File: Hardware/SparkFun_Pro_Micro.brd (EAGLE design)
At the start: 17.8 x 33 mm, 33 parts, among them U2 MIC5219, U3 ATMEGA32U4, Y1 16MHz

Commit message: Proto finished. Add ignore.
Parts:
- removed C13, C19: 10uF, SparkFun:EIA3216
- removed JP6, JP7: (no value), SparkFun:1X12
- removed R5, R7: 22, SparkFun:0603-RES
- removed U2: MIC5219, SparkFun:SOT23-5
- removed X1: (no value), Testing:USB-AB-MICRO-SMD-V03-IN&OUT
- removed Y1: 16MHz, SparkFun:CRYSTAL-SMD-5X3
- added C7, C8: 10uF, SparkFun-Capacitors:0603
- added J1: (no value), USBC:USB-C-16P-4
- added J2: Qwiic, SparkFun-Connectors:JST04_1MM_RA
- added J3, J4: (no value), Castellated:1X12_CASTELLATED
- added LOGO1: SFE_LOGO_NAME_FLAME.1_INCH, SparkFun-Aesthetics:SFE_LOGO_NAME_FLAME_.1
- added LOGO2: QWIIC_LOGO_4MM, SparkFun-Aesthetics:QWIIC_4MM
- added LOGO3: QWIIC_LOGO_6MM, SparkFun-Aesthetics:QWIIC_6MM
- added R1, R3: 5.1k, SparkFun-Resistors:0402-TIGHT
- added R8, R9: 22, SparkFun-Resistors:0402-TIGHT
- added S1: Reset, SparkFun-Switches:TACTILE_SWITCH_SMD_4.6X2.8MM
- added U$10, U$51: (no value), buzzard_labels (15):812
- added U$12, U$46: (no value), buzzard_labels (17):RAW5
- added U$13, U$55: (no value), buzzard_labels (13):45
- added U$14: (no value), buzzard_labels (17):T8
- added U$15, U$33: (no value), buzzard_labels (18):3V39
- added U$16, U$50: (no value), buzzard_labels (15):911
- added U$17, U$37: (no value), buzzard_labels (15):A07
- added U$18, U$60: (no value), buzzard_labels (13):TX2
- added U$19, U$36: (no value), buzzard_labels (15):A18
- added U$2, U$38: (no value), buzzard_labels (15):156
- added U$20: (no value), SparkFun-Aesthetics:PRODUCTION_INSTRUCTIONS
- added U$21, U$49: (no value), buzzard_labels (14):104
- added U$22, U$32: (no value), buzzard_labels (17):GND4
- added U$23: (no value), buzzard_labels (14):MICRO1
- added U$24: (no value), buzzard_labels (14):PRO0
- added U$25: (no value), buzzard_labels (16):RST3
- added U$26, U$35: (no value), buzzard_labels (15):A29
- added U$27, U$34: (no value), buzzard_labels (15):A310
- added U$28, U$59: (no value), buzzard_labels (15):RX20
- added U$29, U$47: (no value), buzzard_labels (15):145
- added U$30: (no value), buzzard_labels (17):R9
- added U$31, U$41: (no value), buzzard_labels (17):RST3
- added U$4, U$48: (no value), buzzard_labels (15):164
- added U$40: (no value), buzzard_labels (18):C5
- added U$43: (no value), buzzard_labels (18):MICRO4
- added U$45: (no value), buzzard_labels (18):PRO3
- added U$5, U$57: (no value), buzzard_labels (15):218
- added U$52, U$9: (no value), buzzard_labels (15):713
- added U$53, U$8: (no value), buzzard_labels (15):614
- added U$54, U$7: (no value), buzzard_labels (15):515
- added U$56, U$6: (no value), buzzard_labels (15):317
- added U$58: (no value), buzzard_labels (16):GND4
- added U1: 3.3V, SparkFun-IC-Power:SOT23-5
- added Y2: 32MHz, SparkFun-Clocks:CRYSTAL-SMD-2.0X1.6MM
- C1, C2, C3, C4: device SparkFun:0603-CAP -> SparkFun-Capacitors:0402-TIGHT
- C10, C5, C6: value 1uF -> 1.0uF; device SparkFun:0603-CAP -> SparkFun-Capacitors:0402-TIGHT
- D1: device SparkFun:LED-0603 -> SparkFun-LED:LED-0603
- D2: value (none) -> 3A/10V/280mV; device SparkFun:SOD-323 -> SparkFun-DiscreteSemi:SOD-323
- D3: value Green -> GREEN; device SparkFun:LED-0603 -> SparkFun-LED:LED-0603
- F1: value 500mA -> 6V 0.5A; device SparkFun:PTC-1206 -> SparkFun-Fuses:0805
- JP1, JP2: value FIDUCIALUFIDUCIAL -> FIDUCIAL1X2; device SparkFun:MICRO-FIDUCIAL -> SparkFun-Aesthetics:FIDUCIAL-1X2
- LED1: value Red -> RED; device SparkFun:LED-0603 -> SparkFun-LED:LED-0603
- R11: value 1K -> 1k; device SparkFun:0603-RES -> SparkFun-Resistors:0402-TIGHT
- R2: value 10K -> 10k; device SparkFun:0603-RES -> SparkFun-Resistors:0402-TIGHT
- R4, R6: value 330 -> 1k; device SparkFun:0603-RES -> SparkFun-Resistors:0402-TIGHT
- SJ1: device SparkFun:SJ_2S -> SparkFun-Jumpers:SMT-JUMPER_2_NO_SILK
- U$1: value LOGO-SFESK -> (none); device SparkFun:SFE-LOGO-FLAME -> buzzard_labels (15):5V21
- U$11: value LOGO-SFENEW -> (none); device SparkFun:SFE-NEW-WEBLOGO -> buzzard_labels (16):GND4
- U$3: value OSHW-LOGOS -> OSHW-LOGOMINI; device SparkFun:OSHW-LOGO-S -> SparkFun-Aesthetics:OSHW-LOGO-MINI
- U3: value ATMEGA32U4 -> ATmega32U4; device Testing:QFN-44-NOPAD_1:1-OUTFAKES -> SparkFun-IC-Microcontroller:QFN-44-NOPAD_1:1
- moved U$3 19.3 mm to (16.3, 31.5), turned to 0 degrees
- moved U$11 18.9 mm to (2.92, 25.1), flipped to the top, turned to 270 degrees
- moved U$1 14.1 mm to (3.17, 33.7), turned to 270 degrees
- moved R2 12.9 mm to (12.4, 17.4), turned to 135 degrees
- moved C6 9.52 mm to (5.21, 19.2), turned to 45 degrees
- moved R4 9.33 mm to (12.7, 6.35), turned to 180 degrees
- moved C2 6.83 mm to (5.71, 9.53), turned to 270 degrees
- moved R6 5.86 mm to (12.7, 7.62), turned to 180 degrees
- moved C4 5.58 mm to (4.19, 9.65), turned to 90 degrees
- moved D3 5.14 mm to (8.89, 7.62), turned to 0 degrees
- moved D1 4.58 mm to (8.89, 6.35), turned to 0 degrees
- moved C10 4.24 mm to (3.81, 12.1), turned to 315 degrees
- moved JP2 3.25 mm to (6.35, 31.8)
- moved D2 3.20 mm to (8.89, 23.4)
- moved LED1 2.37 mm to (4.32, 22.9)
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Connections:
- net D14 renamed RXLED
- net N$4 renamed UCAP
- removed net A4: U3.40
- removed net A5: U3.41
- removed net D11: U3.12
- removed net D12: U3.26
- removed net D13: U3.32
- removed net D2: JP7.8, U3.19
- removed net D3: JP7.7, U3.18
- removed net N$6: R7.2, X1.D-1
- removed net N$8: R5.2, X1.D+1
- removed net UVCC: C6.2, F1.1, U3.2, U3.7, X1.VBUS1
- new net D-_HV: J1.A7, J1.B7, R8.1
- new net D2/SDA: J2.3, J3.8, U3.19
- new net D3/SCL: J2.4, J3.7, U3.18
- new net DP_HV: J1.A6, J1.B6, R9.1
- new net N$10: J1.B5, R1.2
- new net N$9: J1.A5, R3.2
- new net USB_RAW: D2.A, F1.2, SJ1.1
- new net V_USB: C6.2, F1.1, J1.VBUS1, J1.VBUS2, U3.2, U3.7
- net A0: now also J4.8; no longer JP6.8
- net A1: now also J4.7; no longer JP6.7
- net A2: now also J4.6; no longer JP6.6
- net A3: now also J4.5; no longer JP6.5
- net D+: now also R9.2; no longer R5.1
- net D-: now also R8.2; no longer R7.1
- net D10: now also J4.12; no longer JP6.12
- net D4: now also J3.6; no longer JP7.6
- net D5: now also J3.5; no longer JP7.5
- net D6: now also J3.4; no longer JP7.4
- net D7: now also J3.3; no longer JP7.3
- net D8: now also J3.2; no longer JP7.2
- net D9: now also J3.1; no longer JP7.1
- net GND: now also C10.1, C7.1, C8.1, J1.GND, J1.GND2, J2.1, J3.9, J4.2, R1.1, R3.1, S1.1, S1.2, U1.2; no longer C10.2, C13.C, C19.C, JP6.2, JP7.10, JP7.9, U2.2, X1.GND1
- net MISO: now also J4.10; no longer JP6.10
- net MOSI: now also J4.11; no longer JP6.11
- net N$1: now also Y2.1; no longer Y1.1
- net N$2: now also Y2.3; no longer Y1.3
- net N$3: now also J3.10; no longer D2.2, F1.2, SJ1.1
- net RAW: now also C7.2, D2.C, J4.1, U1.1, U1.3; no longer C19.A, D2.1, JP6.1, U2.1, U2.3
- net RESET: now also J4.3, S1.3, S1.4; no longer JP6.3
- net RXI: now also J3.11; no longer JP7.11
- net SCK: now also J4.9; no longer JP6.9
- net TXO: now also J3.12; no longer JP7.12
- net VCC: now also C10.2, C8.2, J2.2, J4.4, U1.5; no longer C10.1, C13.A, JP6.4, U2.5
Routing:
- net UVCC: track 33.6 -> 0.00 mm, vias 4 -> 0
- net D2: track 27.8 -> 0.00 mm, vias 1 -> 0
- net D2/SDA: track 0.00 -> 24.9 mm, vias 0 -> 1
- net V_USB: track 0.00 -> 23.3 mm, vias 0 -> 2
- net D-: track 28.7 -> 6.07 mm
- net D3/SCL: track 0.00 -> 22.6 mm, vias 0 -> 1
- net D+: track 24.6 -> 5.94 mm
- net DP_HV: track 0.00 -> 14.7 mm, vias 0 -> 2
- net D5: track 27.6 -> 13.9 mm
- net USB_RAW: track 0.00 -> 13.5 mm, vias 0 -> 2
- net D-_HV: track 0.00 -> 12.3 mm, vias 0 -> 2
- net GND: track 20.0 -> 8.22 mm, vias 17 -> 25
- net N$3: track 11.1 -> 0.00 mm
- net D6: track 23.2 -> 12.8 mm
- net D3: track 9.86 -> 0.00 mm, vias 1 -> 0
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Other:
- board text added: "0.8mm PCB"
- board text added: "N. Seidle"
- board text added: "v20"
- board text removed: "10"
- board text removed: "14"
- board text removed: "15"
- board text removed: "16"
- board text removed: "2"
- board text removed: "3"
- board text removed: "3.3V"
- board text removed: "3.3V Reg / 8MHz"
- board text removed: "4"
- board text removed: "5"
- board text removed: "5V"
- board text removed: "5V Reg / 16MHz"
- board text removed: "6"
- board text removed: "7"
- board text removed: "8"
- board text removed: "9"
- board text removed: "A0"
- board text removed: "A1"
- board text removed: "A2"
- board text removed: "A3"
- board text removed: "GND"
- board text removed: "J1"
- board text removed: "Mark back accordingly"
- board text removed: "Micro"
- board text removed: "N. Seidle, revised by P. Lewis"
- board text removed: "Pro"
- board text removed: "RAW"
- board text removed: "RST"
- board text removed: "RXI"
- board text removed: "TXO"
- board text removed: "VCC"
- board text removed: "Valid combinations:"
- board text removed: "v13"

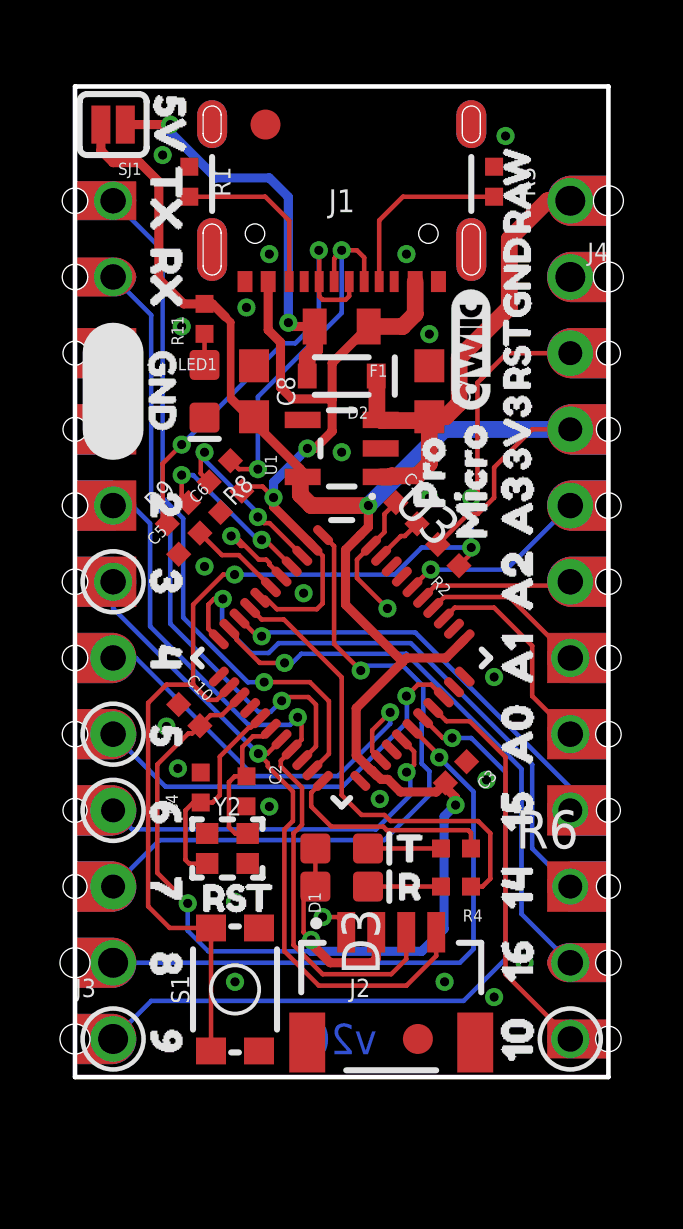
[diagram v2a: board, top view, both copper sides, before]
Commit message: Rev to USB C
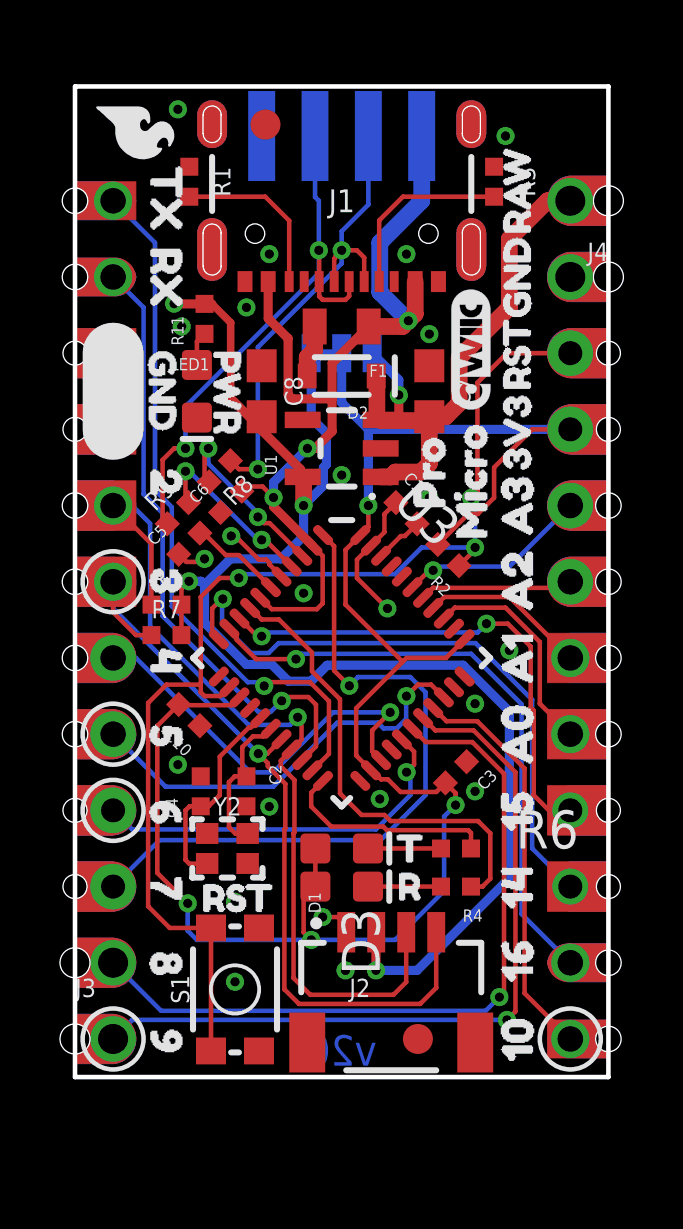
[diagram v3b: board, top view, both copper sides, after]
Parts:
- removed SJ1: Closed for 5V Board, SparkFun-Jumpers:SMT-JUMPER_2_NO_SILK
- added JP14: USB_SOLDER_PADS, SparkFun-Connectors:USB-SOLDER-PADS
- added JP3: (no value), SparkFun-Jumpers:SMT-JUMPER_3_1-NC_TRACE_SILK
- added LOGO4: SFE_LOGO_FLAME.1_INCH, SparkFun-Aesthetics:SFE_LOGO_FLAME_.1
- added R5, R7: 2.2k, SparkFun-Resistors:0402-TIGHT
- added U$39: (no value), buzzard_labels (18):3V39
- added U$42: (no value), buzzard_labels (13):G1
- added U$44: (no value), buzzard_labels (13):V0
- added U$61: (no value), buzzard_labels (14):D#3
- added U$62: (no value), buzzard_labels (14):D#4
- added U$63: (no value), buzzard_labels (10):PWR0
- added U$64: (no value), buzzard_labels (10):5V1
- U$1: device buzzard_labels (15):5V21 -> buzzard_labels (11):VCC1
- moved U$1 11.0 mm to (11.0, 25.9), flipped to the bottom, turned to 0 degrees
- moved U$5 0.76 mm to (3.05, 21.3)
- moved C8 0.25 mm to (6.22, 22.9)
- moved LED1 0.25 mm to (4.06, 22.9)
- moved C4 0.13 mm to (4.19, 9.53)
- moved U$13 0.13 mm to (3.05, 15.4)
- turned C10 to 135 degrees
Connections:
- new net 3.3V: C8.2, J2.2, JP3.3, R11.2, R5.2, R7.2, U1.5
- net D-_HV: now also JP14.D-
- net D2/SDA: now also R5.1
- net D3/SCL: now also R7.1
- net DP_HV: now also JP14.D+
- net GND: now also JP14.GND
- net RAW: now also JP3.1
- net USB_RAW: no longer SJ1.1
- net VCC: now also JP3.2; no longer C8.2, J2.2, R11.2, SJ1.2, U1.5
- net V_USB: now also JP14.VBUS
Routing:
- net 3.3V: track 0.00 -> 48.8 mm, vias 0 -> 4
- net VCC: track 80.6 -> 61.8 mm
- net USB_RAW: track 13.5 -> 1.75 mm, vias 2 -> 0
- net V_USB: track 23.3 -> 30.5 mm, vias 2 -> 3
- net D2/SDA: track 24.9 -> 30.2 mm
- net D8: track 20.4 -> 24.9 mm
- net D3/SCL: track 22.6 -> 26.9 mm
- net D-_HV: track 12.3 -> 16.5 mm
- net DP_HV: track 14.7 -> 18.7 mm
- net SCK: track 14.2 -> 16.9 mm, vias 1 -> 2
- net RAW: track 16.5 -> 19.1 mm, vias 0 -> 1
- net D9: track 23.9 -> 25.6 mm
- net MOSI: track 19.1 -> 20.3 mm
- net MISO: track 19.9 -> 20.9 mm
- net GND: track 8.22 -> 8.90 mm, vias 25 -> 23

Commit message: Commit before ordering v20
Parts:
- removed J1: (no value), USBC:USB-C-16P-4
- added J5: (no value), USBC:USB-C-16P-5
- moved R3 0.25 mm to (13.7, 29.8)
- moved R1 0.25 mm to (4.06, 29.8)
- moved U$18 0.13 mm to (3.05, 31.1)
- turned JP4 to 180 degrees
- renumbered JP3 to JP4
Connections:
- net 3.3V: now also JP4.1; no longer JP4.3
- net D-_HV: now also J5.A7, J5.B7; no longer J1.A7, J1.B7
- net DP_HV: now also J5.A6, J5.B6; no longer J1.A6, J1.B6
- net GND: now also J5.GND, J5.GND2; no longer J1.GND, J1.GND2
- net N$10: now also J5.B5; no longer J1.B5
- net N$9: now also J5.A5; no longer J1.A5
- net RAW: now also JP4.3; no longer JP4.1
- net V_USB: now also J5.VBUS1, J5.VBUS2; no longer J1.VBUS1, J1.VBUS2
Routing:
- net V_USB: track 30.5 -> 31.5 mm
- net N$9: track 6.20 -> 5.45 mm
- net N$10: track 5.69 -> 4.94 mm
- net DP_HV: track 18.7 -> 19.2 mm
- net GND: vias 23 -> 21
